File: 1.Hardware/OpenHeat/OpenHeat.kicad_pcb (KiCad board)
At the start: 2 copper layers, 75 x 50 mm, 48 parts, among them J1 Conn_01x04_Male, J2 Conn_02x05_Odd_Even, J3 Conn_01x04_Female, J4 Conn_01x03_Male, J5 Conn_01x02_Male, M1 Display_Module_I2C, Q1 BC847, Q2 TK8R2E06PL, SW1 Rotary_Encoder_Switch, U1 VXO7803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

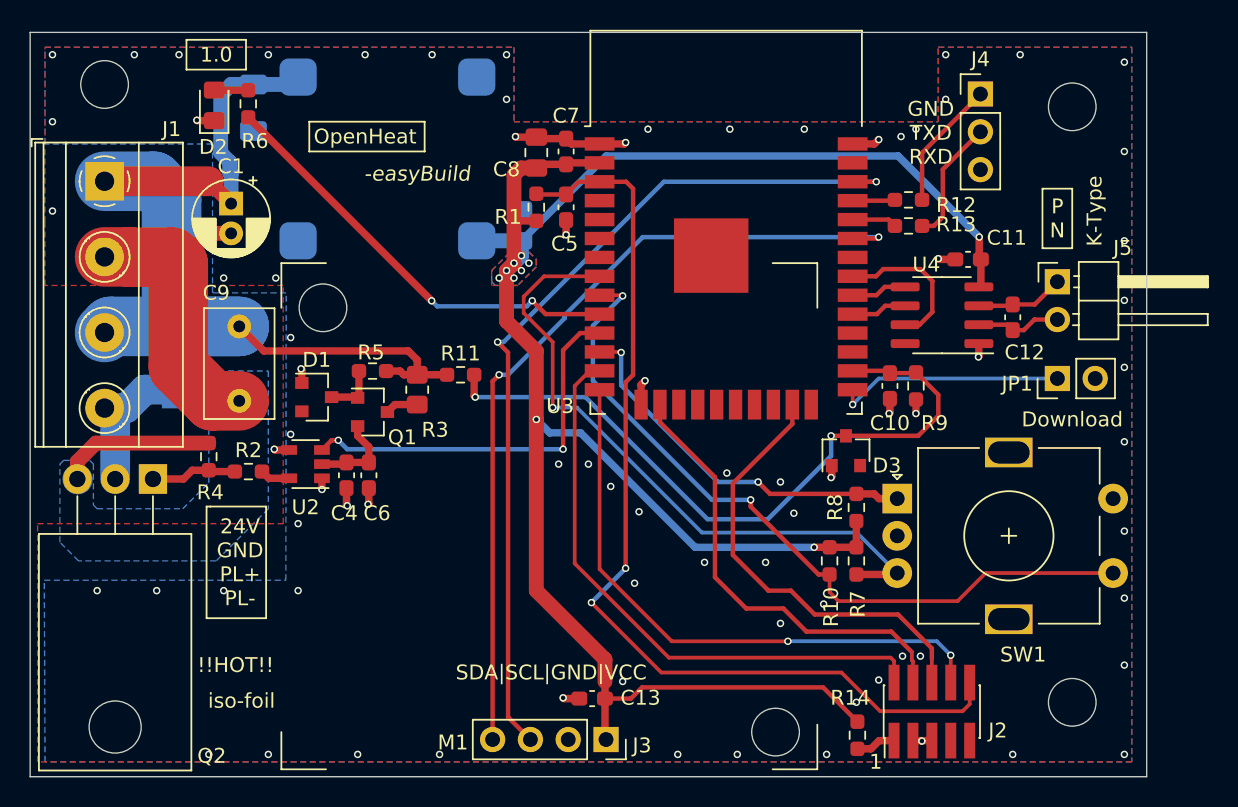
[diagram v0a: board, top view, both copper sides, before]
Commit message: Update OpenHeat.kicad_pcb
Additional VIAs added
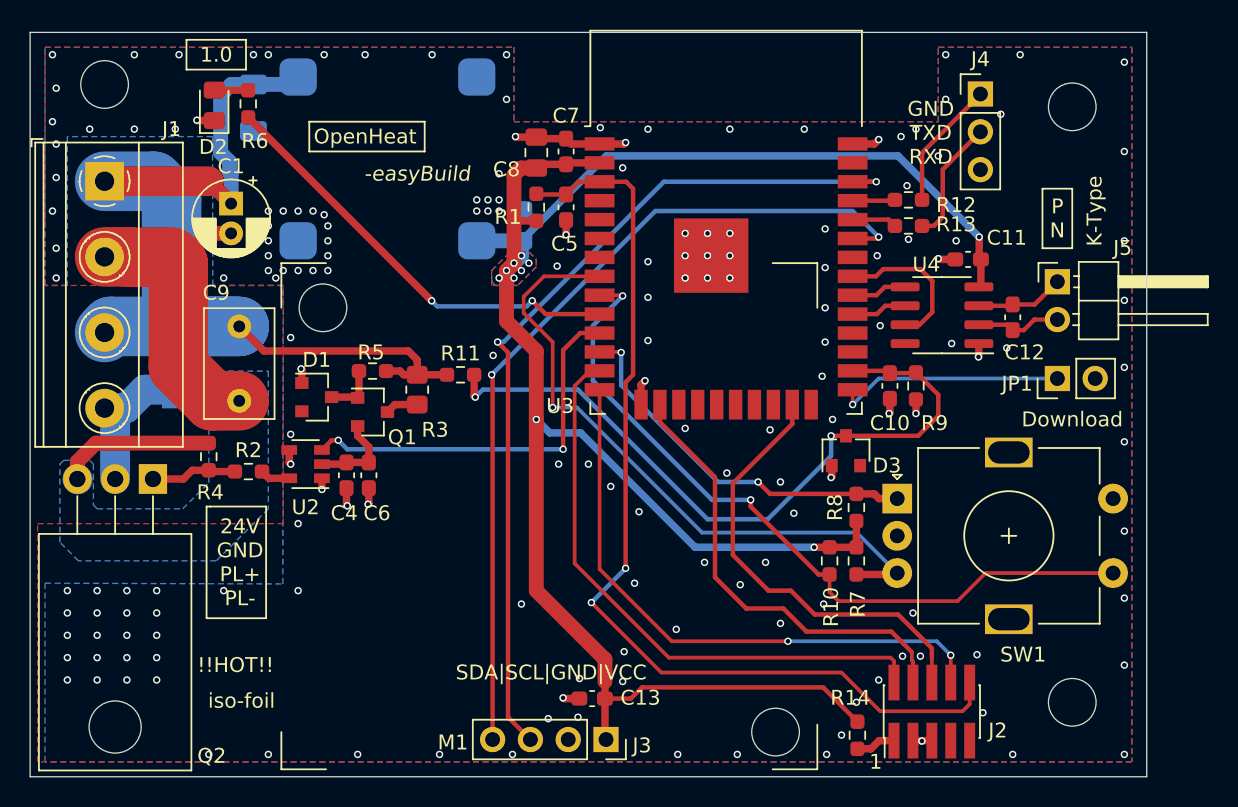
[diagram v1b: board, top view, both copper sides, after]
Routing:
- net /OLED_SDA: track 55.9 -> 57.6 mm
- net GND: track 62.9 -> 62.8 mm, vias 80 -> 176
